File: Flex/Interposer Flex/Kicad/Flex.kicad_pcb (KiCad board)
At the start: 2 copper layers, 99.6 x 58.8 mm, 4 parts

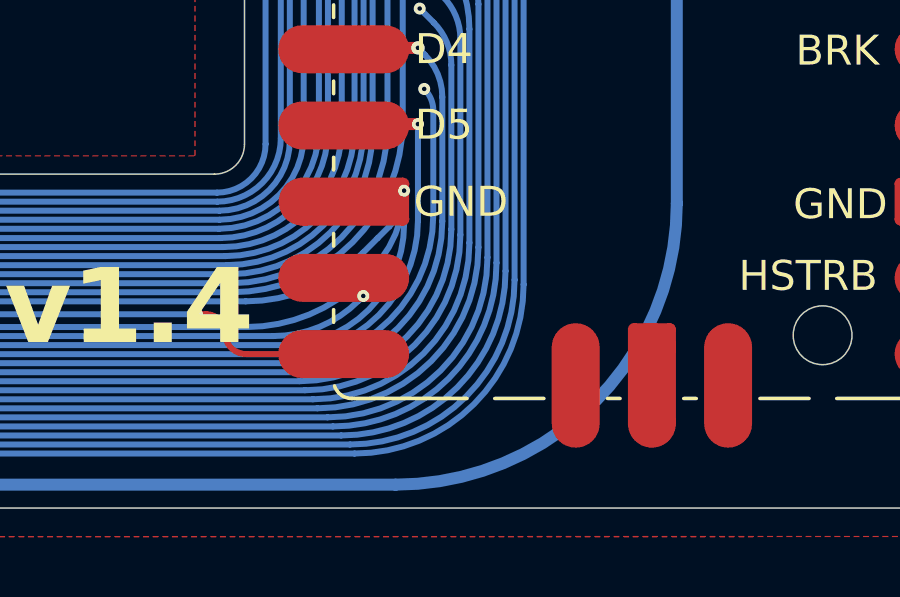
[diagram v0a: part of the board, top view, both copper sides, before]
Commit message: updated silkscreen
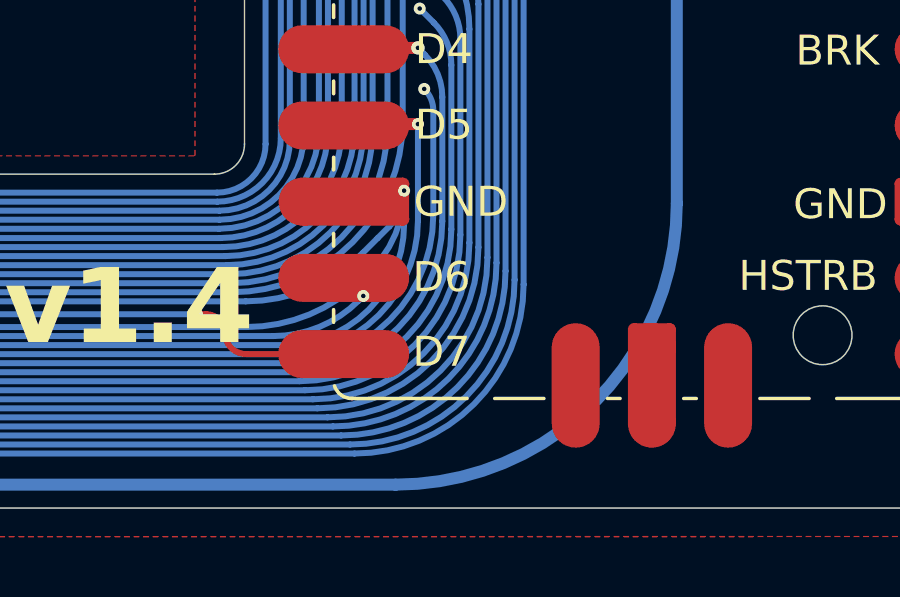
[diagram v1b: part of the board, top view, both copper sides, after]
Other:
- board text added: "D6"
- board text added: "D7"
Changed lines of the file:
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@@
+		)
+	)
+	(gr_text "D7"
+		(at 184.73 105.97 0)
+		(layer "F.SilkS")
+		(effects
+			(font
+				(size 1 1)
+				(thickness 0.1)
+			)
+			(justify left bottom)
 		)
 	)
@@
 		(layer "F.SilkS")
 		(effects
+			(font
+				(size 1 1)
+				(thickness 0.1)
+			)
+			(justify left bottom)
+		)
+	)
+	(gr_text "D6"
+		(at 184.73 103.48 0)
+		(layer "F.SilkS")
+		(effects
